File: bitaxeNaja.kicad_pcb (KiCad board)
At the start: 6 copper layers, 65 x 112 mm, 203 parts, among them J1 XT30, J2 Conn_01x08, J3 Conn_01x04, J4 USB_C_Receptacle_USB2.0, J7 Conn_01x04, SW1 SWITCH-SPST, SW2 SWITCH-SPST, U1 STHW4-DU-HN050206, U10 TLV77308PDBVR, U11 TLV77312PDBVR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

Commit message: AGND and OSNS
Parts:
- removed C10: 1uF, Capacitor_SMD:C_0603_1608Metric
- added C21: 1uF, Capacitor_SMD:C_0402_1005Metric, B.Cu at (134.7, 86.4)
- added NT2: NetTie_1, bitaxe:NetTie-2_SMD_Pad0.2mmx1mm, B.Cu at (135.6, 91.5)
- added NT5: NetTie_2, bitaxe:NetTie-2_SMD_Pad0.2mmx1mm, B.Cu at (158.2, 95.5)
- added NT6: NetTie_2, bitaxe:NetTie-2_SMD_Pad0.2mmx1mm, B.Cu at (159.0, 94.5)
- added TP4: CLKI, TestPoint:TestPoint_Pad_D1.0mm, B.Cu at (114.5, 109.8)
- moved R7 2.75 mm to (138.7, 91.9)
- moved R8 2.54 mm to (137.7, 91.9)
- moved C18 2.54 mm to (138.2, 90.4)
- moved C11 1.28 mm to (133.8, 87.4), turned to 180 degrees
- moved R5 0.19 mm to (132.7, 86.5)
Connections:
- R7 pad 1: /VDD -> /Power/OSNS+
- R8 pad 2: GND -> /Power/OSNS-
- U3 pad 37: GND -> /Power/AGND
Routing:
- net /Power/OSNS-: track 0.00 -> 24.0 mm, vias 0 -> 2
- net /Power/OSNS+: track 0.00 -> 22.1 mm, vias 0 -> 2
- net /Power/AGND: track 0.00 -> 6.36 mm, vias 0 -> 2
- net GND: track 42.3 -> 37.9 mm, vias 464 -> 463
- net Net-(U3-GOSNS): track 5.48 -> 2.98 mm
- net Net-(U3-VOSNS): track 6.75 -> 4.25 mm
- net Net-(U3-AVIN): track 5.37 -> 3.79 mm, vias 2 -> 0
- net /Power/V5reg_1: track 2.60 -> 1.51 mm
- net /ESP32/SMB_ALRT: track 47.1 -> 48.1 mm
- net /ESP32/SCL: track 80.1 -> 80.8 mm
- net /ESP32/SDA: track 77.9 -> 78.5 mm

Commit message: cleaned up kicad trailing whitespace warnings and normalized capacitor units
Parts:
- moved C2 0.42 mm to (128.3, 79.7)
- moved C3 0.35 mm to (128.3, 81.3)
- moved C110 0.27 mm to (128.3, 82.8)
- moved C4 0.24 mm to (128.3, 85.7)
- moved C111 0.20 mm to (128.3, 84.4)
- moved C5 0.16 mm to (128.3, 86.7)
- moved C6 0.11 mm to (128.3, 87.7)
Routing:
- net GND: vias 463 -> 462

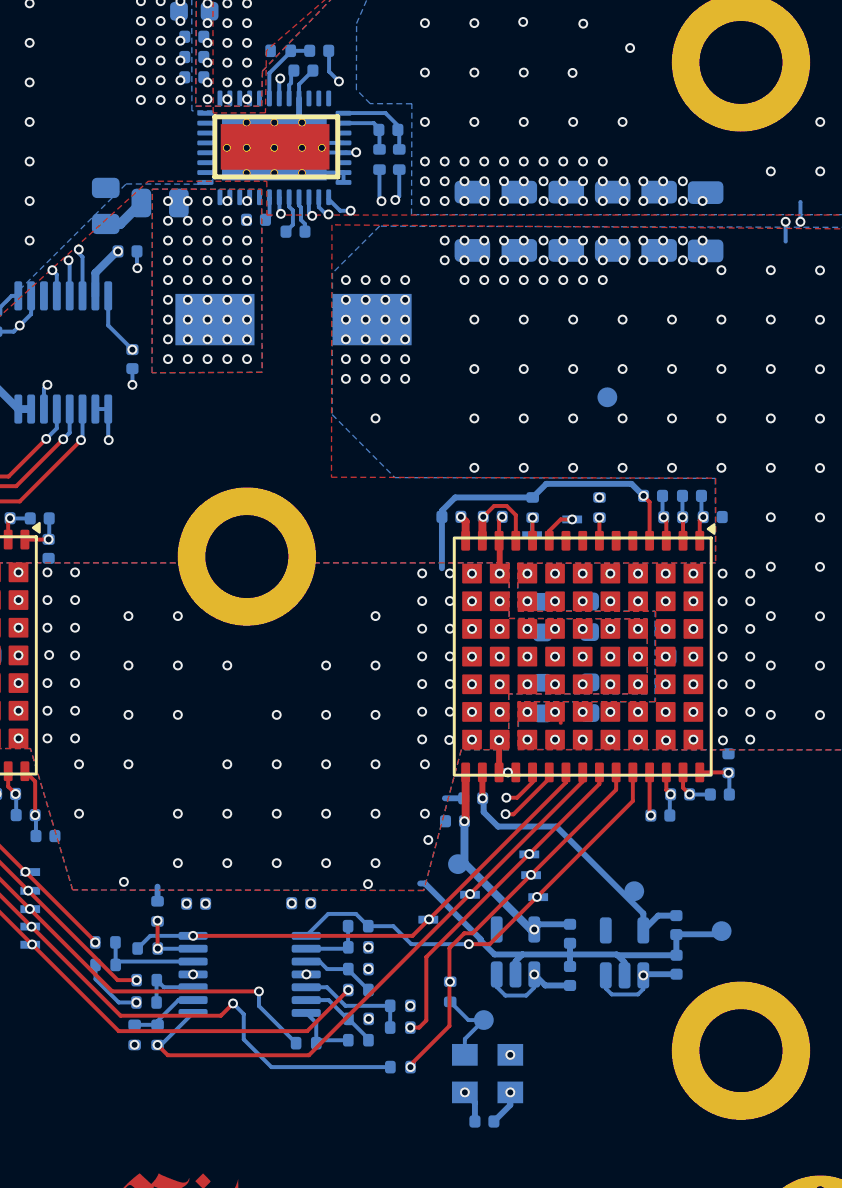
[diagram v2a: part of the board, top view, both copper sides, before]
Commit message: footprint, BOM cleanup. bypass capacitor spacing cleanup
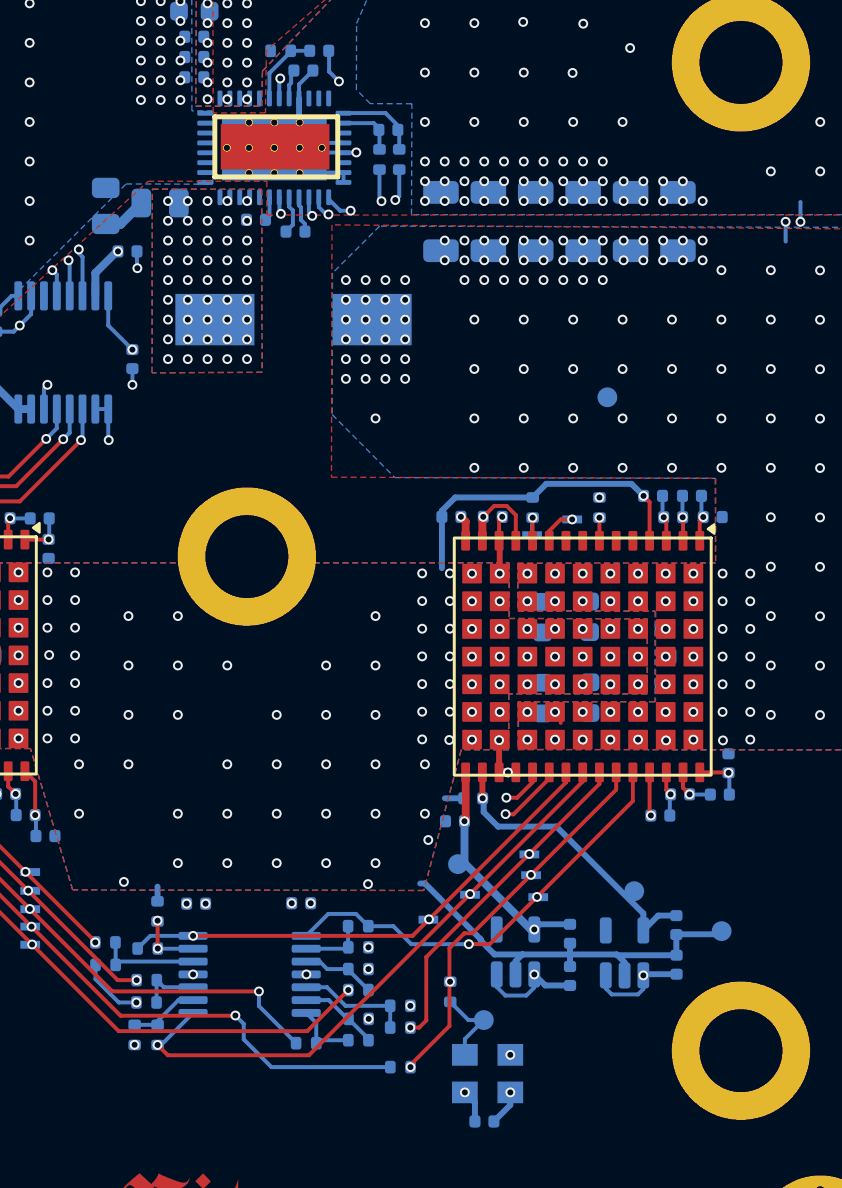
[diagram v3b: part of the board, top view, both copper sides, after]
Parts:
- C22, C23: value 100nf -> 0.1uF
- moved C9 1.59 mm to (140.8, 95.0)
- moved C13 1.57 mm to (143.2, 95.0)
- moved C14 1.54 mm to (145.6, 95.0)
- moved C19 1.50 mm to (148.0, 95.0)
- moved C20 1.45 mm to (150.4, 95.0)
- moved C100 1.40 mm to (152.8, 95.0)
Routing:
- net /ASIC/Level Shifter/CLKI: track 32.8 -> 32.0 mm
